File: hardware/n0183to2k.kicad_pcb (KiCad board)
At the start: 2 copper layers, 60 x 60 mm, 41 parts, among them J1 NMEA0183 (wind), J2 Conn_01x06_Male, J3 Conn_01x05_Male, J4 RJ45, J5 RJ45, J6 Conn_02x03_Odd_Even, Q1 BSS123, Q2 DMG2307L, Q3 BSS123, U1 PIC18F27Q84_ISS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

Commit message: replace a SMD resistor with a though-hole to avoid a jumper, and finish routing
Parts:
- R7: footprint Resistor_SMD:R_0805_2012Metric_Pad1.20x1.40mm_HandSolder -> Resistor_THT:R_Axial_DIN0207_L6.3mm_D2.5mm_P7.62mm_Horizontal; moved to F.Cu
- moved R7 2.87 mm to (111.2, 109.0), turned to 90 degrees
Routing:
- net GND: track 420.9 -> 484.9 mm
- net +3V3: track 106.7 -> 128.2 mm, vias 2 -> 4
- net Net-(J4-Pad7): track 54.5 -> 53.7 mm
- net Net-(J4-Pad8): track 52.7 -> 51.9 mm

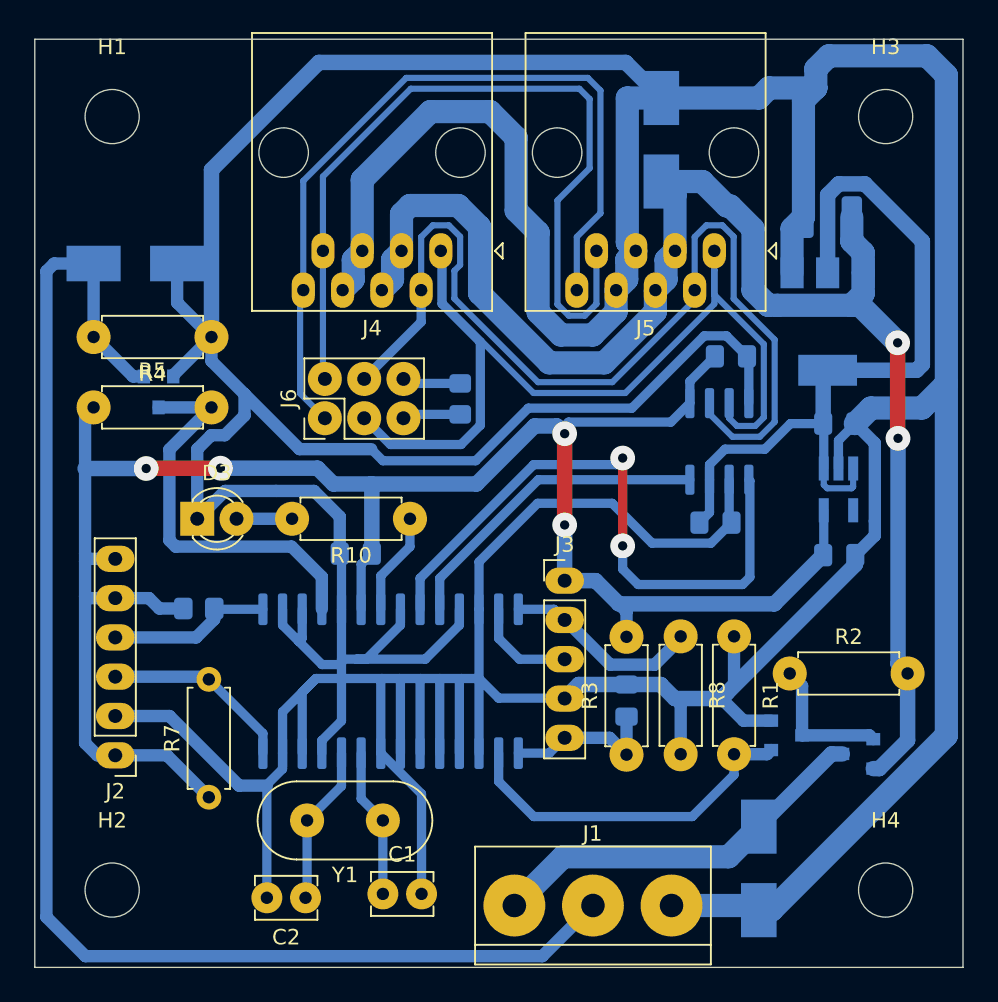
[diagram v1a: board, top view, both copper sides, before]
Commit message: reomve GND nets and add a GND zone
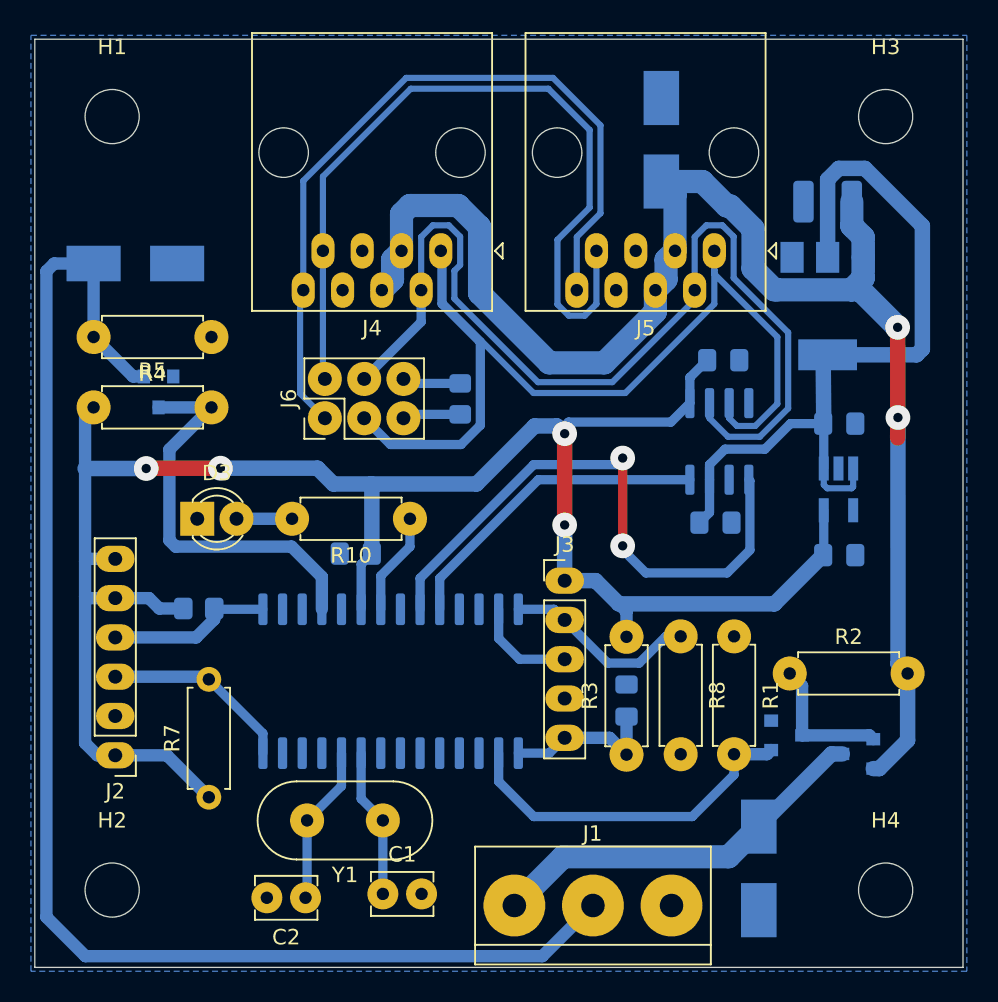
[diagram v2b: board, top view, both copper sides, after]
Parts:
- moved C9 1.00 mm to (151.2, 70.5)
- moved U4 1.00 mm to (151.2, 77.2)
- moved C4 0.56 mm to (144.5, 80.8)
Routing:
- net GND: track 484.9 -> 0.00 mm
- net /CANTX: track 40.7 -> 38.3 mm
- net +12V: track 96.9 -> 98.6 mm
- net +5V: track 49.9 -> 51.4 mm
- net Net-(J4-Pad8): track 51.9 -> 50.6 mm
- net Net-(J4-Pad7): track 53.7 -> 52.5 mm
- net /CANL: track 64.2 -> 65.1 mm
- net /CANH: track 64.7 -> 65.5 mm
- added copper zone on B.Cu, net GND

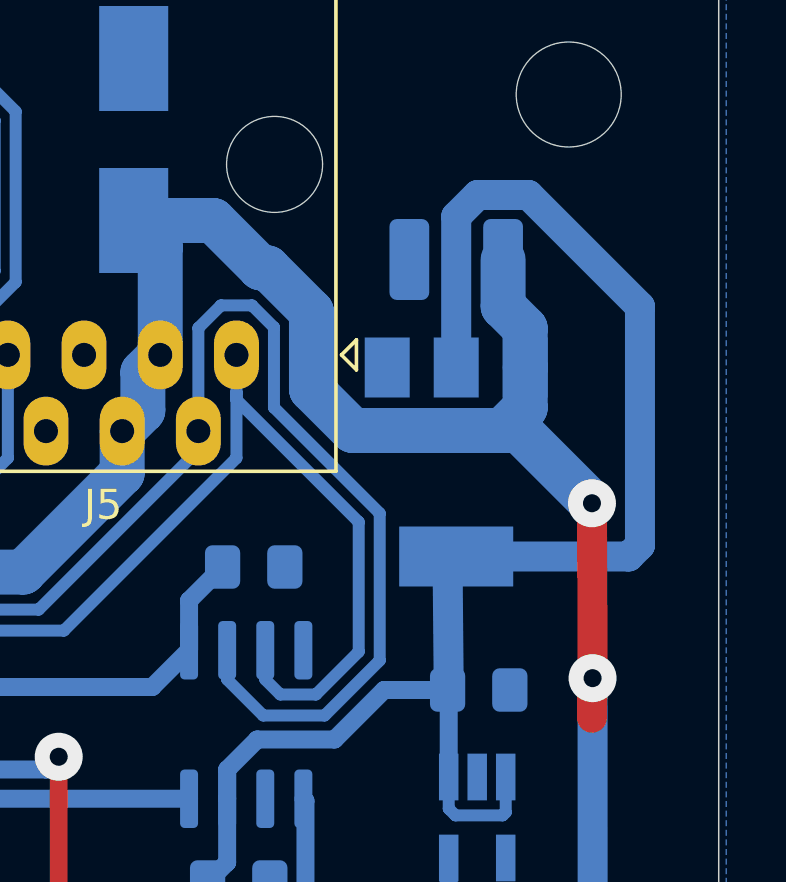
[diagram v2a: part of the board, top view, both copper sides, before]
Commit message: More strait routing for U4
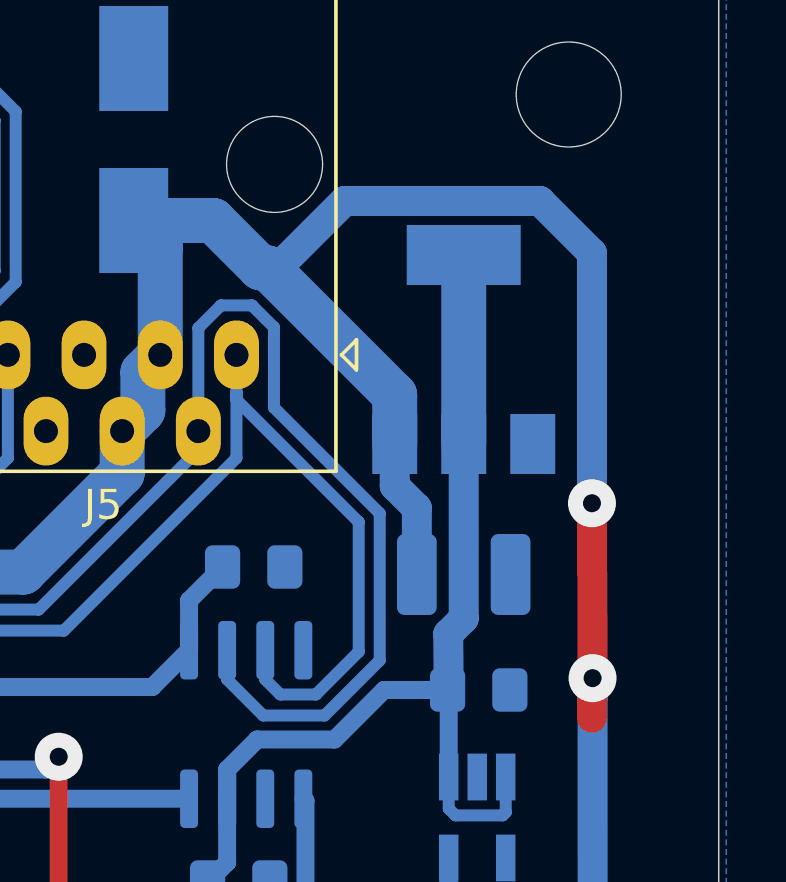
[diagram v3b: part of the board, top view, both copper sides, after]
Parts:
- moved C9 10.5 mm to (151.5, 81.0), turned to 0 degrees
- moved U4 3.76 mm to (151.5, 73.5), turned to 90 degrees
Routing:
- net +5V: track 51.4 -> 34.3 mm
- net +12V: track 98.6 -> 107.9 mm

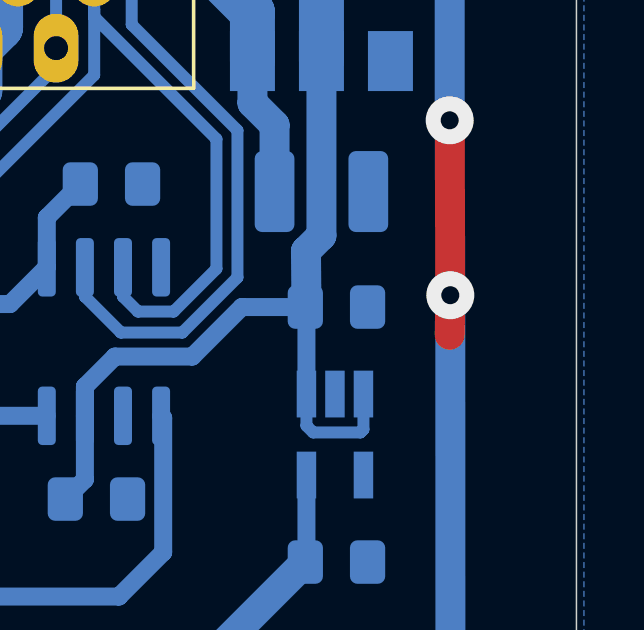
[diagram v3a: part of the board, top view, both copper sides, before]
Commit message: Cosmetic fix on a jumper
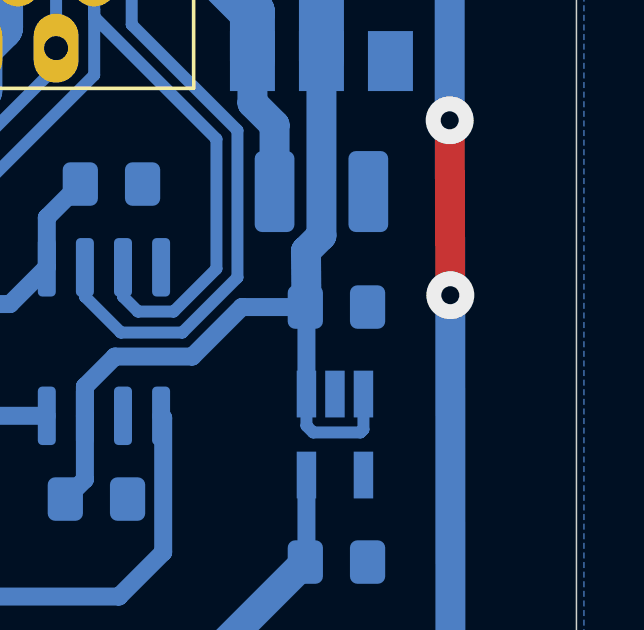
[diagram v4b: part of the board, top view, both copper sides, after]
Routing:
- net +12V: track 107.9 -> 106.6 mm

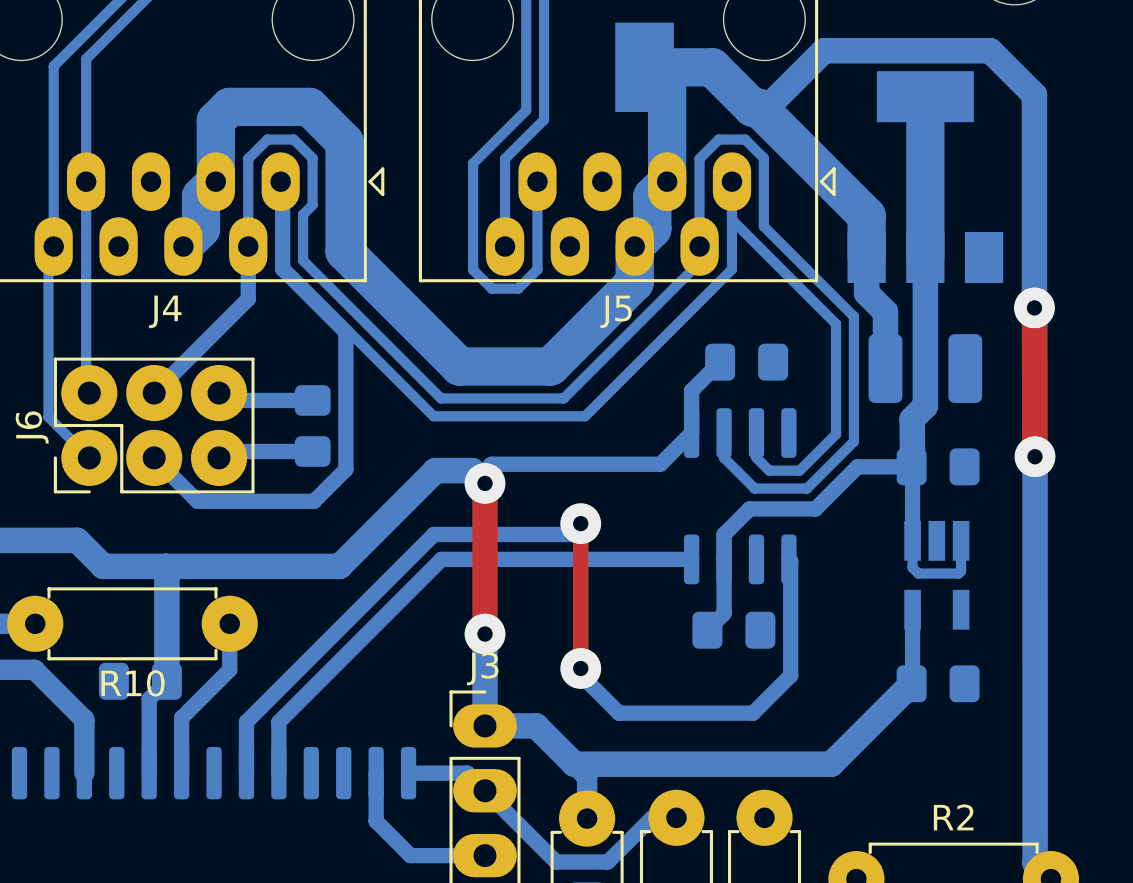
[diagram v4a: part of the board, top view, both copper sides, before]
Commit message: move a jumper from a signal trace to GND. Other misc. improvements
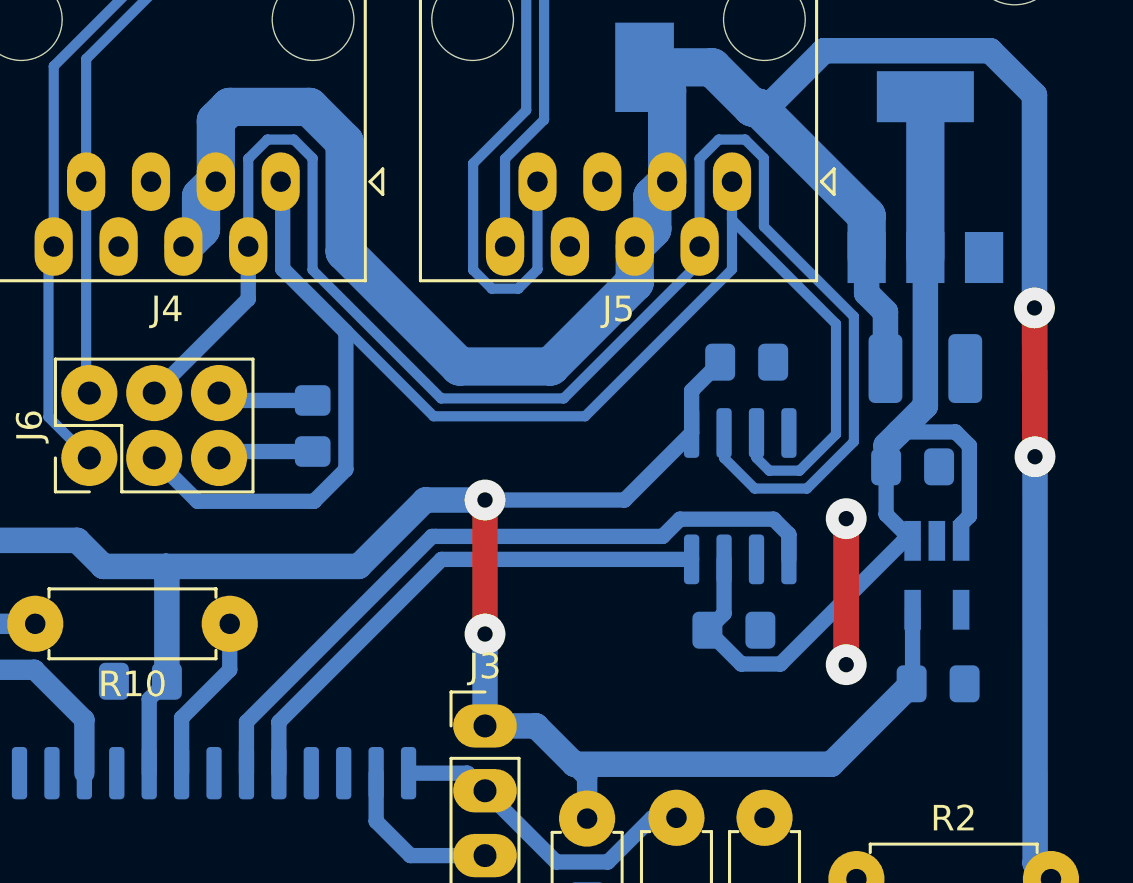
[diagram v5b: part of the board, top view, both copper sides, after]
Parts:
- moved C8 1.00 mm to (151.0, 84.8)
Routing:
- net /CANTX: track 38.3 -> 27.8 mm, vias 2 -> 0
- net GND: track 0.00 -> 5.72 mm, vias 0 -> 2
- net +5V: track 34.3 -> 38.9 mm
- net +3V3: track 127.8 -> 126.2 mm
